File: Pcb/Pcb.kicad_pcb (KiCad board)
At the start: 2 copper layers, 152.3 x 104.7 mm, 123 parts, among them J1 TRRS, Q1 2N7002, SW1 SW_Push, SW10 SW_Push, SW11 SW_Push, SW12 SW_Push, SW13 SW_Push, SW14 SW_Push, SW15 SW_Push, SW16 SW_Push, SW17 SW_Push, SW18 SW_Push, SW19 SW_Push, SW2 SW2, SW20 SW_Push, SW21 SW_Push, SW22 SW_Push, SW23 SW_Push, SW24 SW_Push, SW25 SW_Push, SW26 SW_Push, SW27 SW_Push, SW28 SW_Push, SW29 SW_Push, SW3 SW_Push, SW4 SW_Push, SW5 SW_Push, SW6 SW_Push, SW7 SW_Push, SW8 SW_Push, SW9 SW_Push, U1 ProMicro

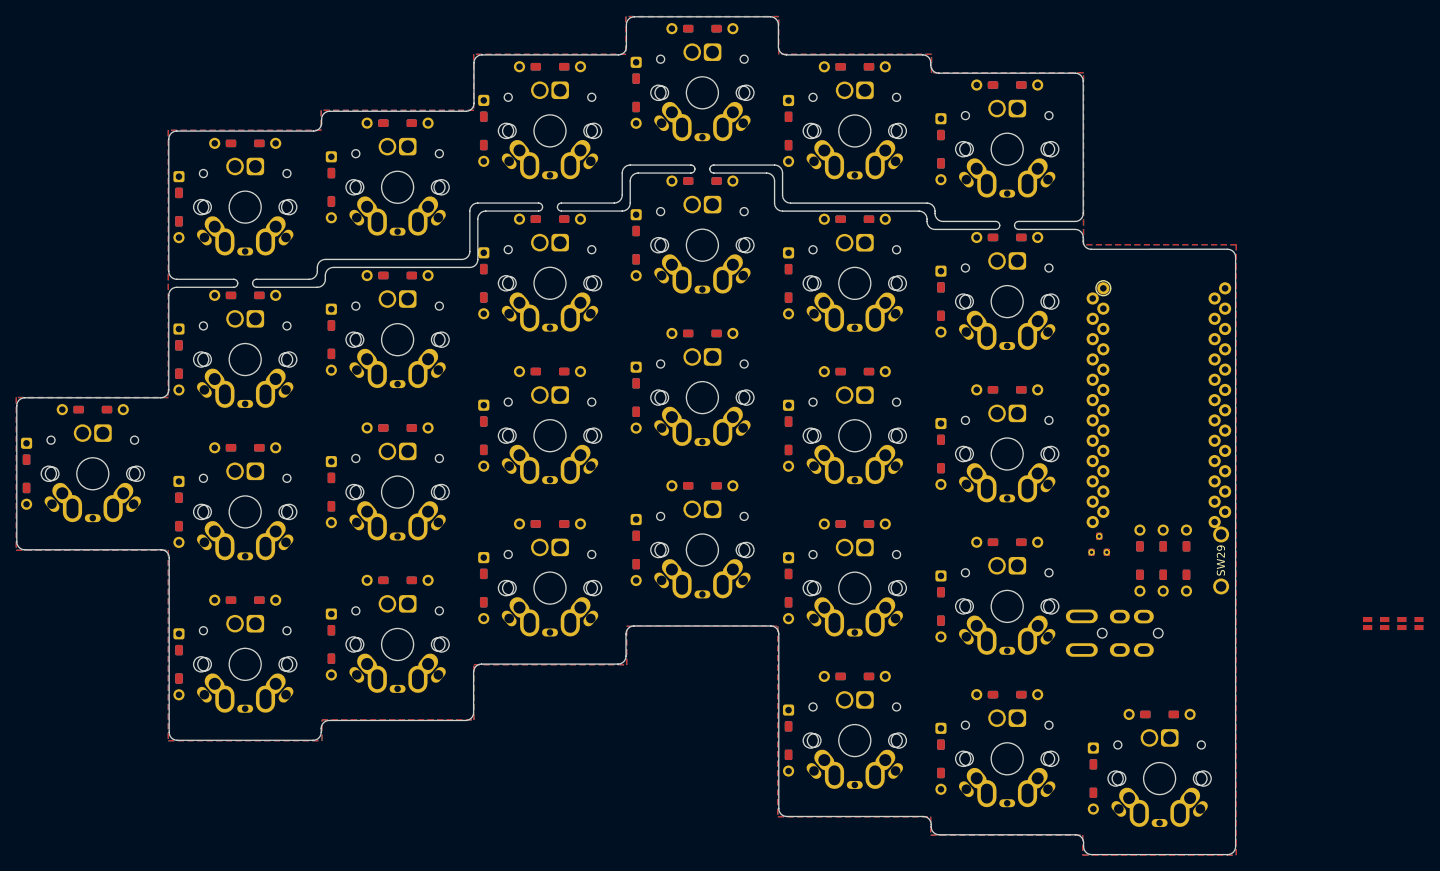
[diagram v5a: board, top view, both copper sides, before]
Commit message: Placed hole in correct position
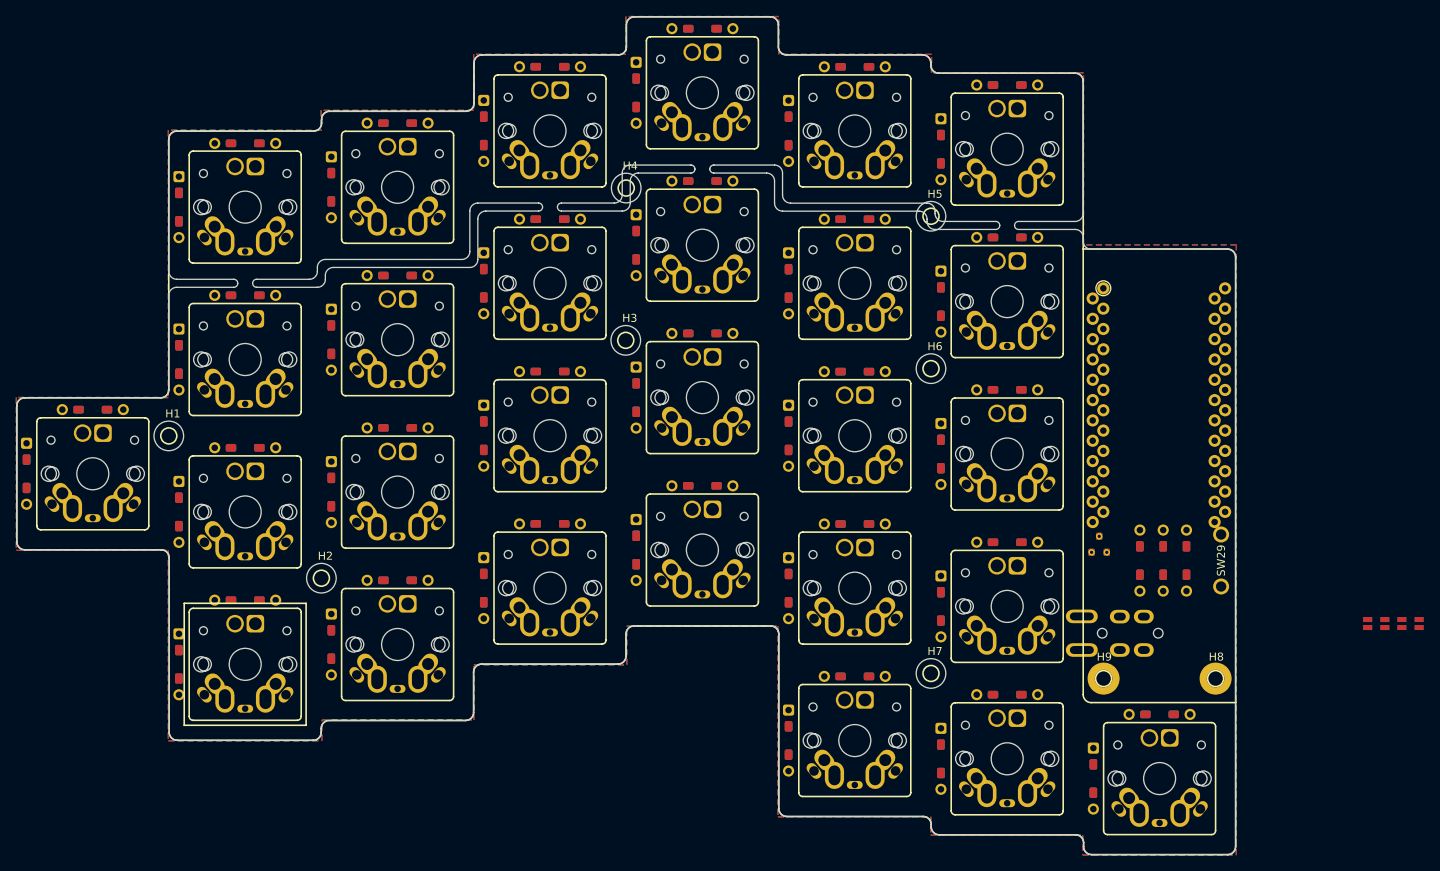
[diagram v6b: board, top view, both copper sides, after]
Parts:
- added H1: CaseHole, Used_Footprints:MountHole, F.Cu at (96.2, 82.5)
- added H2: CaseHole, Used_Footprints:MountHole, F.Cu at (115.2, 100.3)
- added H3: CaseHole, Used_Footprints:MountHole, F.Cu at (153.3, 70.6)
- added H4: CaseHole, Used_Footprints:MountHole, F.Cu at (153.3, 51.5)
- added H5: CaseHole, Used_Footprints:MountHole, F.Cu at (191.4, 55.0)
- added H6: CaseHole, Used_Footprints:MountHole, F.Cu at (191.4, 74.1)
- added H7: CaseHole, Used_Footprints:MountHole, F.Cu at (191.4, 112.2)
- added H8: CoverHole, Used_Footprints:CoverHole, F.Cu at (227.0, 112.8)
- added H9: CoverHole, Used_Footprints:CoverHole, F.Cu at (213.0, 112.8)

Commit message: Update
Deleted silkscreen, moved jumpers and some components
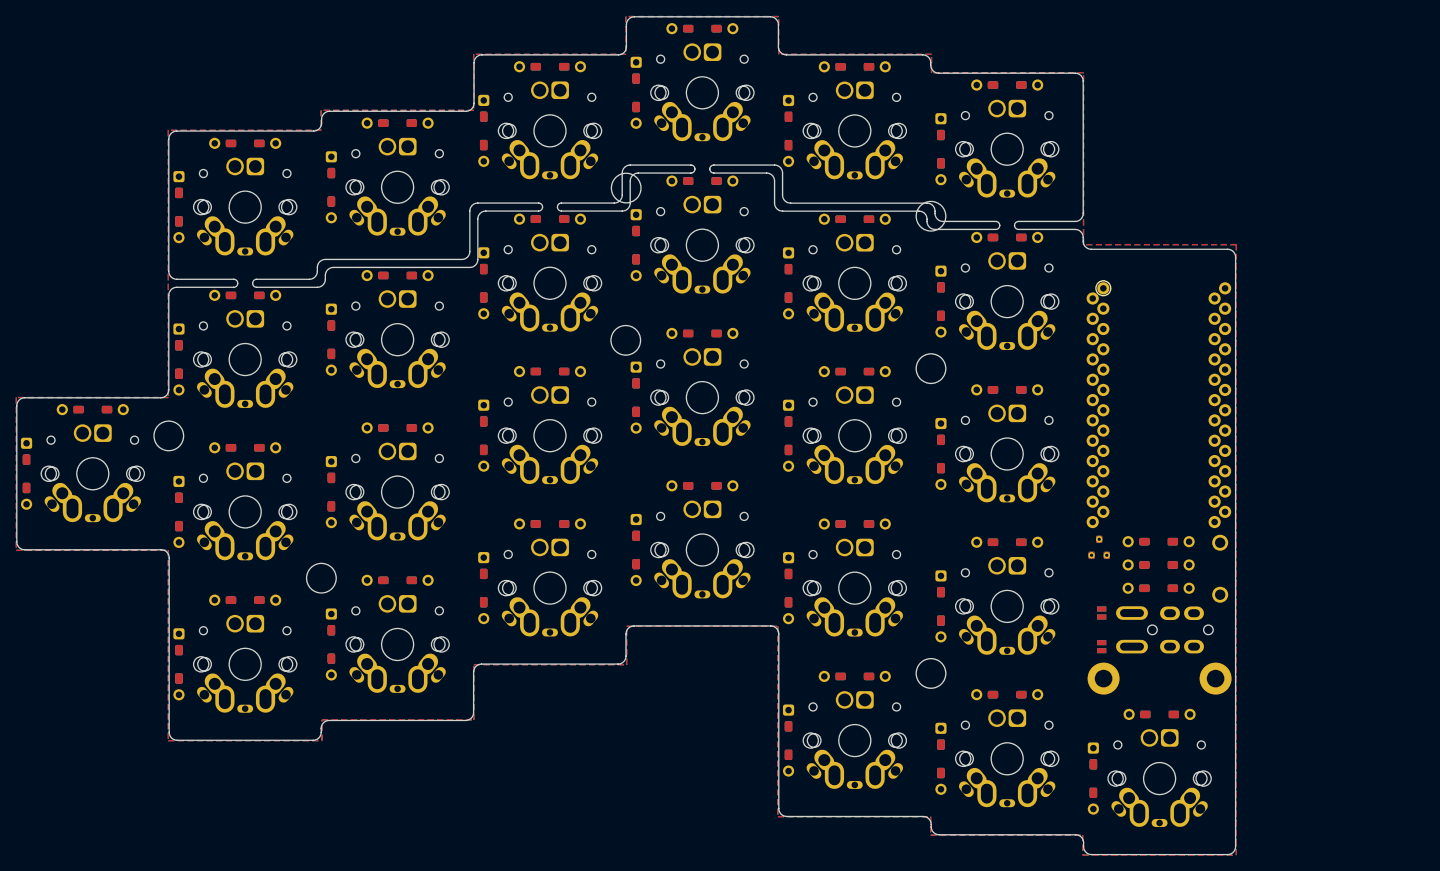
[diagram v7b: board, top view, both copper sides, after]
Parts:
- J1: footprint 1symblos:MJ-4PP-9_Dual -> Used_Footprints:TRSS_DUAL
- JP2, JP5: moved to B.Cu
- moved JP5 39.8 mm to (212.8, 108.8)
- moved JP4 37.6 mm to (212.8, 108.8), turned to 180 degrees
- moved JP3 35.4 mm to (212.8, 104.6)
- moved JP2 33.3 mm to (212.8, 104.6), turned to 180 degrees
- moved J1 6.28 mm to (227.6, 106.7)
- moved R30 4.91 mm to (219.9, 101.5), turned to 180 degrees
- moved R31 3.32 mm to (219.9, 95.7), turned to 0 degrees
- moved SW29 1.04 mm to (227.6, 99.1)
- moved R29 0.79 mm to (219.9, 98.6), turned to 0 degrees
- moved Q1 0.37 mm to (212.4, 96.5)

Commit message: Update
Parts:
- added G***: LOGO, 1symblos:Jiran_Silk_Sign, B.Cu at (219.9, 77.3)
- added G***: LOGO, 1symblos:Jiran_Silk_Sign, F.Cu at (219.9, 77.3)
